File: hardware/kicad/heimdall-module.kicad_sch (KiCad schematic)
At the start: 20 parts, among them U1 MC33269DT-3.3G, U2 2.4GHz, U3 TYPEC-214-ARP14H105

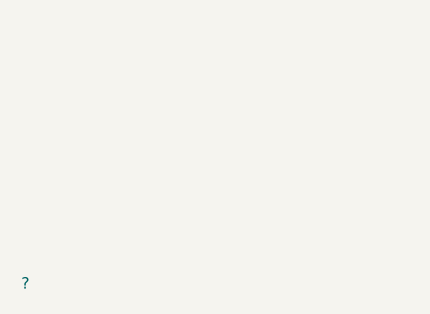
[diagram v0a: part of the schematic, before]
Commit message: Sync the imported PCB with the schematic and clean up ERC
After Update PCB from Schematic, the pads were on the new hierarchical
nets (/VCC, /SDA, ...) but tracks, vias and zones kept the old names;
moved them over. Removed EasyEDA's A4 frame symbol and empty Field42
properties. Gave pins real types: passives, connectors and diode are
passive, MC33269 Vin/Vout are power in/out, ESP32 IOs bidirectional.
GND is now a KiCad power symbol. ERC is down from 100 to 19 and DRC from
167 to 92; what is left is design and layout, not import.

Co-Authored-By: Claude Opus 5.5 <noreply@anthropic.com>
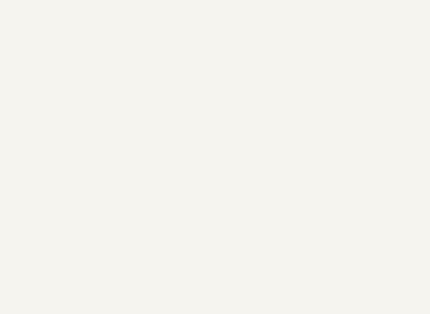
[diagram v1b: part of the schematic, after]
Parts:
- removed ?: (no value), heimdall-m-easyedapro:, symbol heimdall-m-easyedapro:Drawing-Symbol_A4

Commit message: Schematic revision: strapping, decoupling, ESD, reverse feed, breakout
- IO2 and IO8 had no pull-ups. Espressif's checklist needs IO2 high for
  every boot mode and IO8 high for download boot. Added 10k pull-ups
  (R11, R12), plus a 10k pull-up on IO9 (R13, recommended) and a solder
  jumper to GND (JP1 BOOT) for forcing download mode.
- EN delay cap C4: 100nF -> 1uF (Espressif: 10k + 1uF).
- C5 10uF tantalum at the module's 3V3 pin. The regulator's 10uF (C2) is
  ~25mm of trace away, and the MC33269 datasheet warns against low-ESR
  ceramics close to its output, hence tantalum.
- C1 (LDO input) tantalum -> 1uF 50V X7R ceramic: no ESR need on the
  input, and no tantalum surge failure on hot-plug.
- D2 between the bay's VBAT pin (now VBAT_IN) and the regulator input, so
  USB power can't flow into the radio's battery rail.
- U4 USBLC6-2SC6 ESD protection on USB D+/D-/VBUS.
- J2: the loose breakout pads become a 2x4 header symbol (GND, 3V3, SDA,
  SCL, IO3, IO10, IO7, pin 8 free). RXD/TXD stubs removed (no-connect).
- PWR_FLAGs, trimmed EasyEDA wire stubs. ERC: 0 violations.

PCB not updated yet.

Co-Authored-By: Claude Opus 5.5 <noreply@anthropic.com>
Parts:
- added C5: 10uF, heimdall-m-easyedapro:CASE-A_3216, symbol heimdall-m-easyedapro:T491A106K010AT_C1508940
- added D2: 1N5819, heimdall-m-easyedapro:SMA_L4.4-W2.6-LS5.0-RD, symbol heimdall-m-easyedapro:1N5819_C437199
- added J2: Breakout, Connector_PinHeader_2.54mm:PinHeader_2x04_P2.54mm_Vertical, symbol Connector_Generic:Conn_02x04_Odd_Even
- added JP1: BOOT, Jumper:SolderJumper-2_P1.3mm_Open_RoundedPad1.0x1.5mm, symbol Jumper:SolderJumper_2_Open
- added R11, R12, R13: 10kΩ, heimdall-m-easyedapro:R0805, symbol heimdall-m-easyedapro:ERJP06F1002V
- added U4: USBLC6-2SC6, Package_TO_SOT_SMD:SOT-23-6, symbol heimdall-m-easyedapro:USBLC6-2SC6
- C1: value 330nF -> 1uF; footprint heimdall-m-easyedapro:CAP-SMD_L3.2-W1.6 -> heimdall-m-easyedapro:C0805; symbol heimdall-m-easyedapro:T491A334K035AT -> heimdall-m-easyedapro:GRM21B7U1A104JA01L; LCSC Part Name 330nF ±10% 35V -> (none); Manufacturer KEMET(基美) -> Murata; Manufacturer Part T491A334K035AT -> GCM21BR71H105KA03L; Supplier LCSC -> TME; Supplier Part C212667 -> GCM21BR71H105KA03L
- C4: value 100nF -> 1uF; LCSC Part Name 100nF ±5% 10V -> (none); Manufacturer muRata(村田) -> Murata; Manufacturer Part GRM21B7U1A104JA01L -> GCM21BR71H105KA03L; Supplier LCSC -> TME; Supplier Part C710980 -> GCM21BR71H105KA03L
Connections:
- net GND: now also C5.2, J2.1 (Pin_1), JP1.2 (B), U4.2 (GND)
- net IO10: now also J2.6 (Pin_6)
- net IO3: now also J2.5 (Pin_5)
- net IO7: now also J2.7 (Pin_7)
- net SCL: now also J2.4 (Pin_4)
- net SDA: now also J2.3 (Pin_3)
- net USB-D+: now also U4.1 (I/O1), U4.6 (I/O1)
- net USB-D-: now also U4.3 (I/O2), U4.4 (I/O2)
- net VBAT: now also D2.1 (C); no longer H1.3
- net VBUS: now also U4.5 (VBUS)
- net VCC: now also C5.1, J2.2 (Pin_2), R11.2, R12.2, R13.2
- net IO2: now reaches U2.16 (IO2)
- net IO2: now also R11.1
- net IO8: now reaches U2.7 (IO8)
- net IO8: now also R12.1
- net IO9: now reaches U2.8 (IO9)
- net IO9: now also JP1.1 (A), R13.1
- net RXD: no longer names the net of U2.11 (RXD)
- net TXD: no longer names the net of U2.12 (TXD)
- new net VBAT_IN: D2.2 (A), H1.3
- no-connect marks 0 -> 3

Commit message: Rev 2: corrected schematic, re-placed and re-routed board
Schematic (on top of the previous commit):
- I2C moved from IO0/IO1 to GPIO20/21 and bay SIGNAL/DATA swapped onto
  IO4/IO5, so the right-hand pins can reach J2 without crossing the 3V3
  trunk. No firmware exists yet. SCL sits on U0TXD (boot log); SDA stays a
  pulled-up input, so no I2C start condition happens at boot. The console
  has to use USB-Serial/JTAG.
- JP1 kept out of BOM/position files; U2 value -> part name.

PCB:
- H1 slot restored: EasyEDA had it as a multi-layer fill (became copper
  in the import). Now a 12.7 x 2.03mm cut-out, H1's pads trimmed to end
  0.5mm before it.
- All copper rebuilt: power class 0.6mm (VBUS, VBAT, VBAT_IN), 3V3 trunk
  0.5mm (Espressif: >= 20 mil), signals 0.25mm, 0.2mm clearance,
  0.7/0.3 and 0.8/0.4 vias. No via touches a pad (checked).
- U1 tab heatsink copper on both layers, vias beside the tab, not in it.
- No tracks/vias on top under the module body (GND only).
- Vertical USB-C: round 0.7mm pads (0.6mm square gave a 0.09mm ring);
  the pin field (VBUS, CC, D+/D- crossover) laid by hand.
- GND pours on both layers, stitched; a GND track along the module's
  bottom pad row joins the right-hand side to the rest.
- Edited footprints written back to the project library.
- route_pcb.py (adapted from heimdall-switch) and rev_pcb.py record how it
  was made.

ERC 0. DRC 0 errors, 0 unconnected, 0 parity; 1 warning (U3 A1 thermal
relief on top has one spoke; the pad also joins the bottom pour).

Co-Authored-By: Claude Opus 5.5 <noreply@anthropic.com>
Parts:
- JP1: now left out of the parts list
- U2: value 2.4GHz -> ESP32-C3-WROOM-02-N4
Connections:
- net DATA: now also R6.1; no longer R5.1
- net SCL: now also U2.12 (TXD); no longer U2.17 (IO1)
- net SDA: now also U2.11 (RXD); no longer U2.18 (IO0)
- net SIGNAL: now also R5.1; no longer R6.1
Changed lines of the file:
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@@
 	(wire
 		(pts
-			(xy 160.02 45.72) (xy 158.75 45.72)
-		)
-		(stroke
-			(width 0)
-			(type default)
-		)
-	)
-	(wire
-		(pts
 			(xy 186.69 60.96) (xy 186.69 63.5)
 		)
@@
 	(wire
 		(pts
-			(xy 165.1 50.8) (xy 149.86 50.8)
-		)
-		(stroke
-			(width 0)
-			(type default)
-		)
-	)
-	(wire
-		(pts
 			(xy 45.72 90.17) (xy 48.26 90.17)
 		)
@@
 	(wire
 		(pts
-			(xy 158.75 48.26) (xy 149.86 48.26)
-		)
-		(stroke
-			(width 0)
-			(type default)
-		)
-	)
-	(wire
-		(pts
-			(xy 158.75 45.72) (xy 158.75 48.26)
-		)
-		(stroke
-			(width 0)
-			(type default)
-		)
-	)
-	(wire
-		(pts
 			(xy 101.6 120.65) (xy 76.2 120.65)
 		)
@@
 		)
 	)
-	(label "DATA"
+	(label "SIGNAL"
 		(at 99.06 83.82 90)
 		(effects
@@
 		)
 	)
-	(label "SIGNAL"
+	(label "DATA"
 		(at 105.41 83.82 90)
 		(effects
@@
 			)
 		)
-		(property "Value" "2.4GHz"
+		(property "Value" "ESP32-C3-WROOM-02-N4"
 			(at 132.08 73.66 0)
 			(show_name no)
@@
 		(body_style 0)
 		(exclude_from_sim no)
-		(in_bom yes)
+		(in_bom no)
 		(on_board yes)
-		(in_pos_files yes)
+		(in_pos_files no)
 		(dnp no)
 		(property "Reference" "JP1"
@@
 	)
 	(no_connect
-		(at 149.86 66.04)
+		(at 149.86 48.26)
 	)
 	(no_connect
-		(at 149.86 63.5)
+		(at 149.86 50.8)
+	)
+	(label "SDA"
+		(at 149.86 66.04 0)
+		(effects
+			(font
+				(size 1.27 1.27)
+			)
+			(justify left bottom)
+		)
+	)
+	(label "SCL"
+		(at 149.86 63.5 0)
+		(effects
+			(font
+				(size 1.27 1.27)
+			)
+			(justify left bottom)
+		)
 	)
 	(sheet_instances
